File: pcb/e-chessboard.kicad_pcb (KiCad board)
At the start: 2 copper layers, 170 x 170 mm, 54 parts, among them J1 POWER, J2 UART, Q1 BC847, Q2 BC847, SW1 Reset, SW2 Boot, U1 ESP32-WROOM-32U, U2 AOZ1280, U3 NCV7608

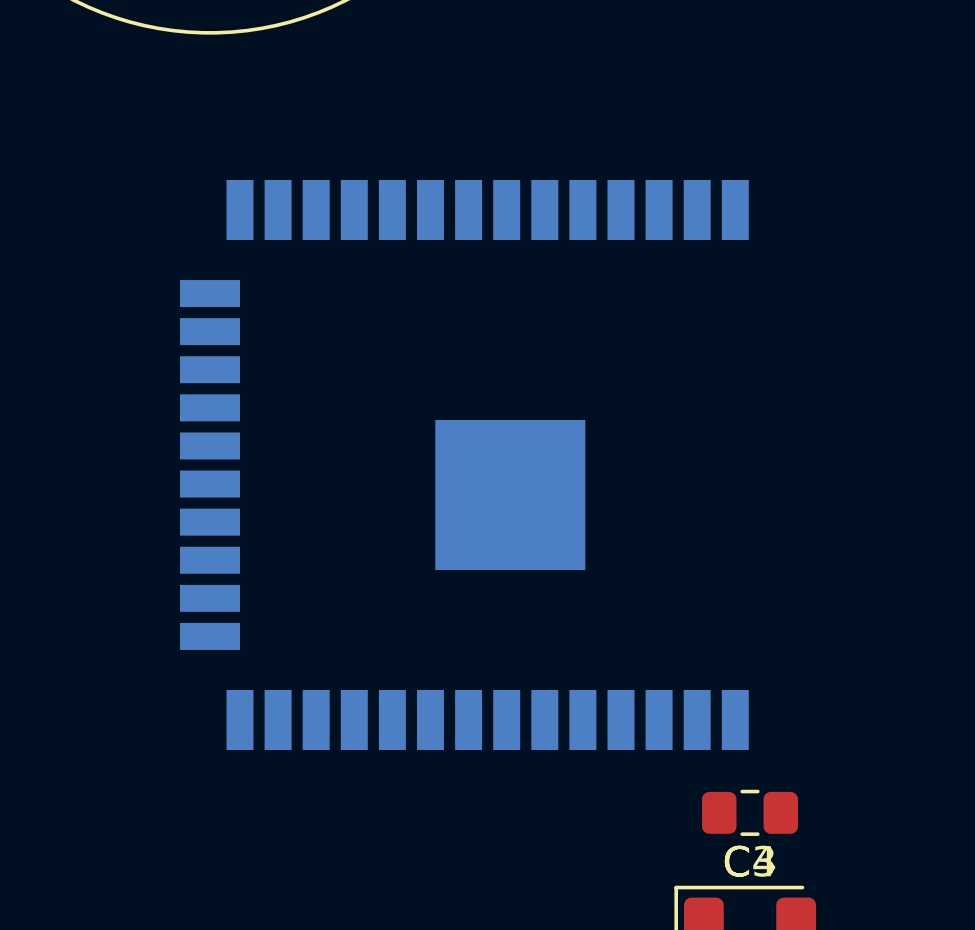
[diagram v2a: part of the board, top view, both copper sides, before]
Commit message: fix(kicad): fixing pin order of pwm
Adjusting the pin order of the pwm lines for better line laying.
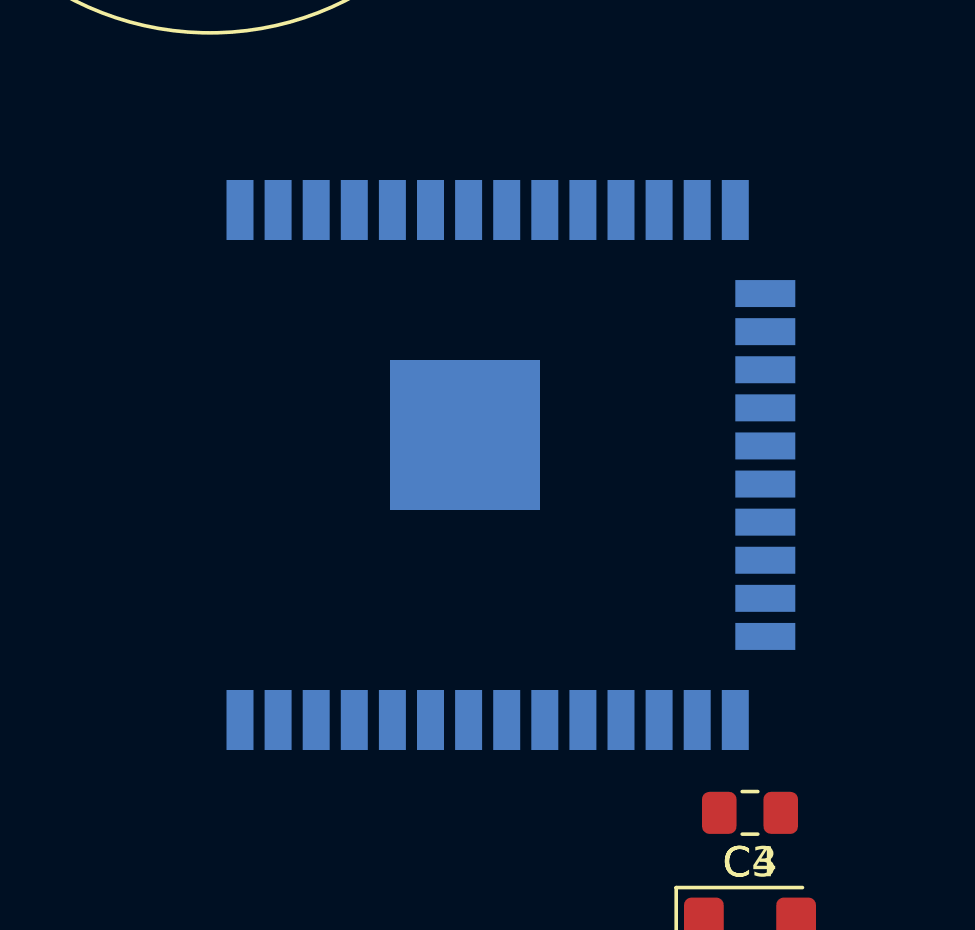
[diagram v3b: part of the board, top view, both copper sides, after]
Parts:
- turned U1 to 270 degrees
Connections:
- U1 pad 12: MAG_PWM_ROW3 -> MAG_PWM_ROW1
- U1 pad 8: MAG_PWM_ROW1 -> MAG_PWM_ROW3

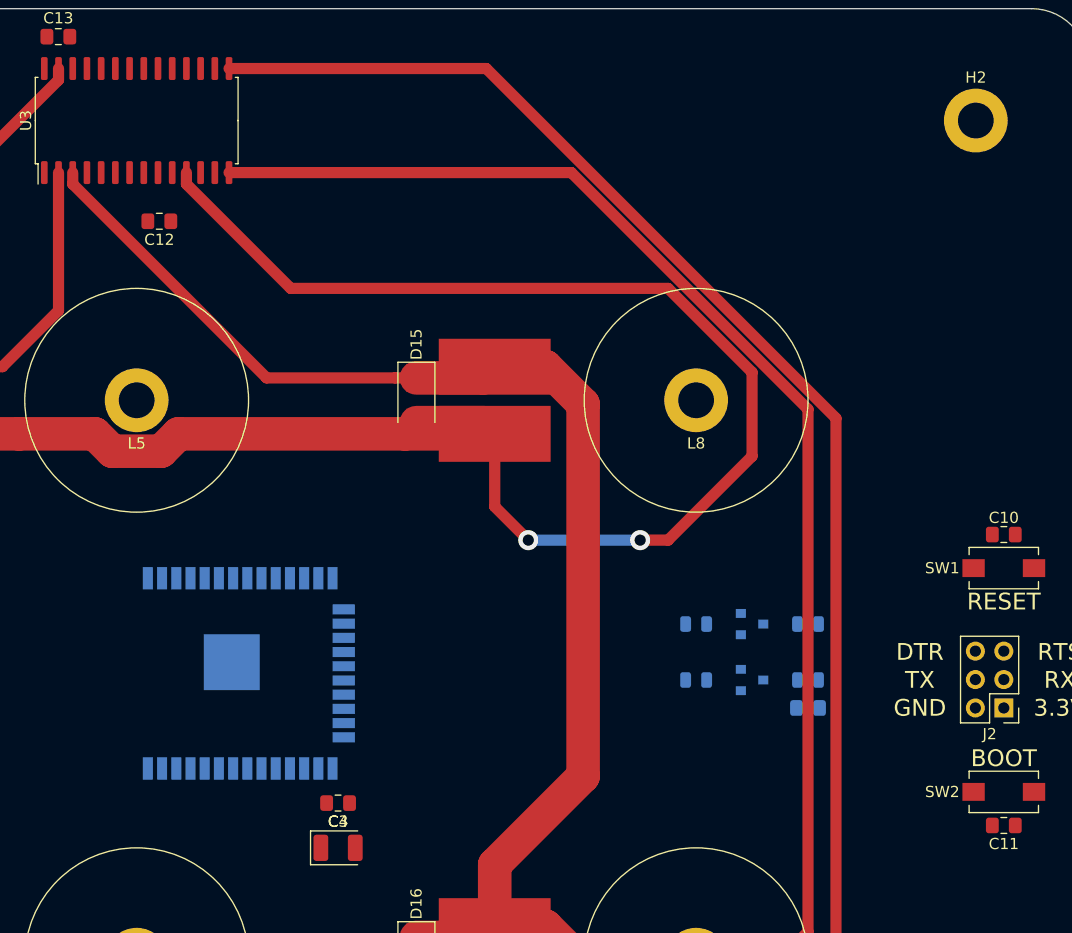
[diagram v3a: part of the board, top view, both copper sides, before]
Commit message: feat(kicad): wireing mosfet driver
Completly wirering the mosfet driver ic.
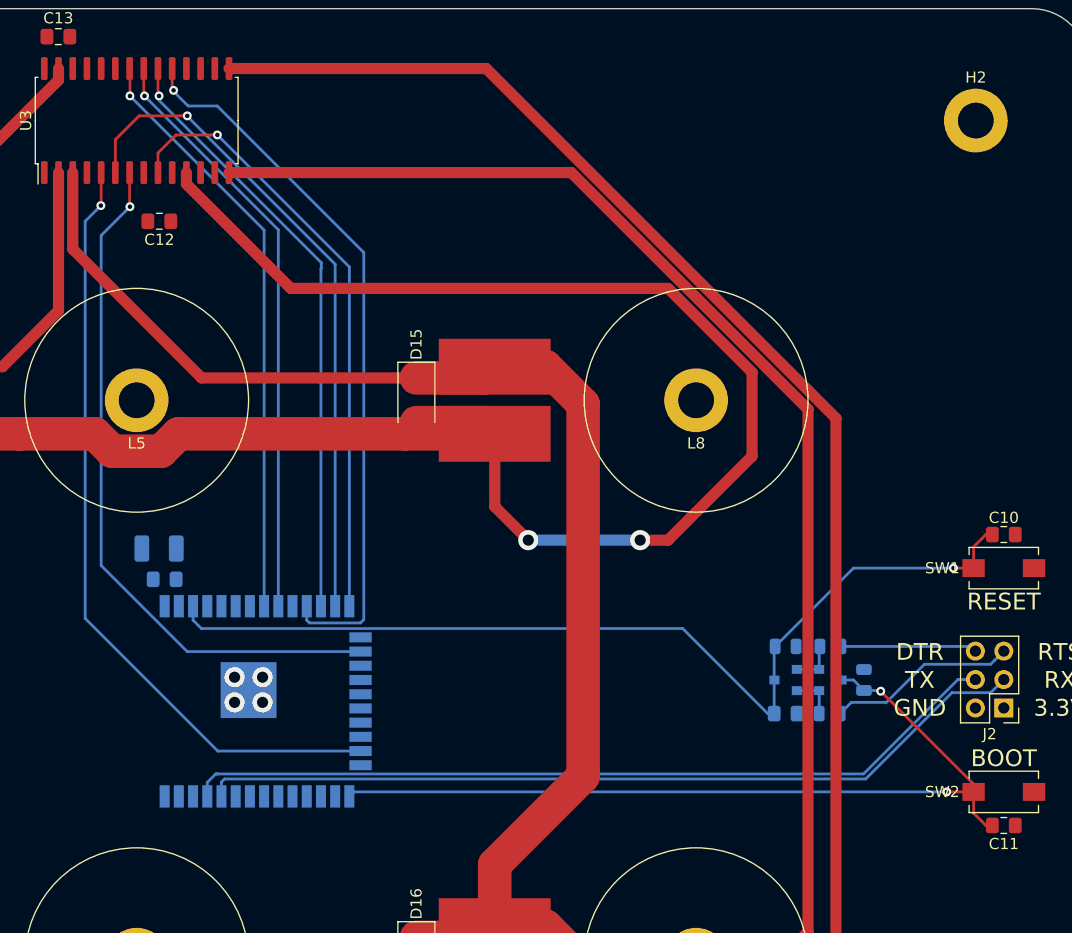
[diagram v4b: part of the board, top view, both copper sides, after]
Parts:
- C3, C4: moved to B.Cu
- moved C3 31.2 mm to (137.0, 98.2), turned to 180 degrees
- moved C4 25.3 mm to (137.5, 101.0), turned to 0 degrees
- moved R2 14.4 mm to (196.9, 113.0), turned to 0 degrees
- moved R1 12.4 mm to (197.0, 107.0), turned to 0 degrees
- moved Q2 8.60 mm to (197.0, 110.0)
- moved R6 7.07 mm to (200.0, 110.0), turned to 90 degrees
- moved R5 3.61 mm to (193.0, 107.0), turned to 0 degrees
- moved Q1 3.00 mm to (193.0, 110.0), turned to 180 degrees
- moved U1 2.92 mm to (145.8, 111.9)
- moved C9 2.06 mm to (193.0, 113.0), turned to 0 degrees
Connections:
- U1 pad 11: (no net) -> MAG_EN
- U1 pad 27: MAG_EN -> (no net)
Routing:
- net EN: track 0.00 -> 87.3 mm, vias 0 -> 1
- net IO0: track 0.00 -> 76.3 mm, vias 0 -> 2
- net UART_RX: track 0.00 -> 75.0 mm
- net UART_TX: track 0.00 -> 73.7 mm
- net MAG_CS: track 0.00 -> 70.0 mm, vias 0 -> 1
- net MAG_EN: track 0.00 -> 64.4 mm, vias 0 -> 1
- net MOSI: track 0.00 -> 62.6 mm, vias 0 -> 1
- net SCLK: track 0.00 -> 59.6 mm, vias 0 -> 1
- net MISO: track 0.00 -> 54.7 mm, vias 0 -> 1
- net MAG_PWM_ROW1: track 0.00 -> 54.1 mm, vias 0 -> 1
- net MAG_PWM_ROW2: track 0.00 -> 53.0 mm, vias 0 -> 1
- net MAG_PWM_ROW3: track 0.00 -> 53.0 mm, vias 0 -> 1
- net RTS: track 0.00 -> 16.9 mm
- net DTR: track 0.00 -> 12.2 mm
- net Net-(Q1-Pad1): track 0.00 -> 4.08 mm
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
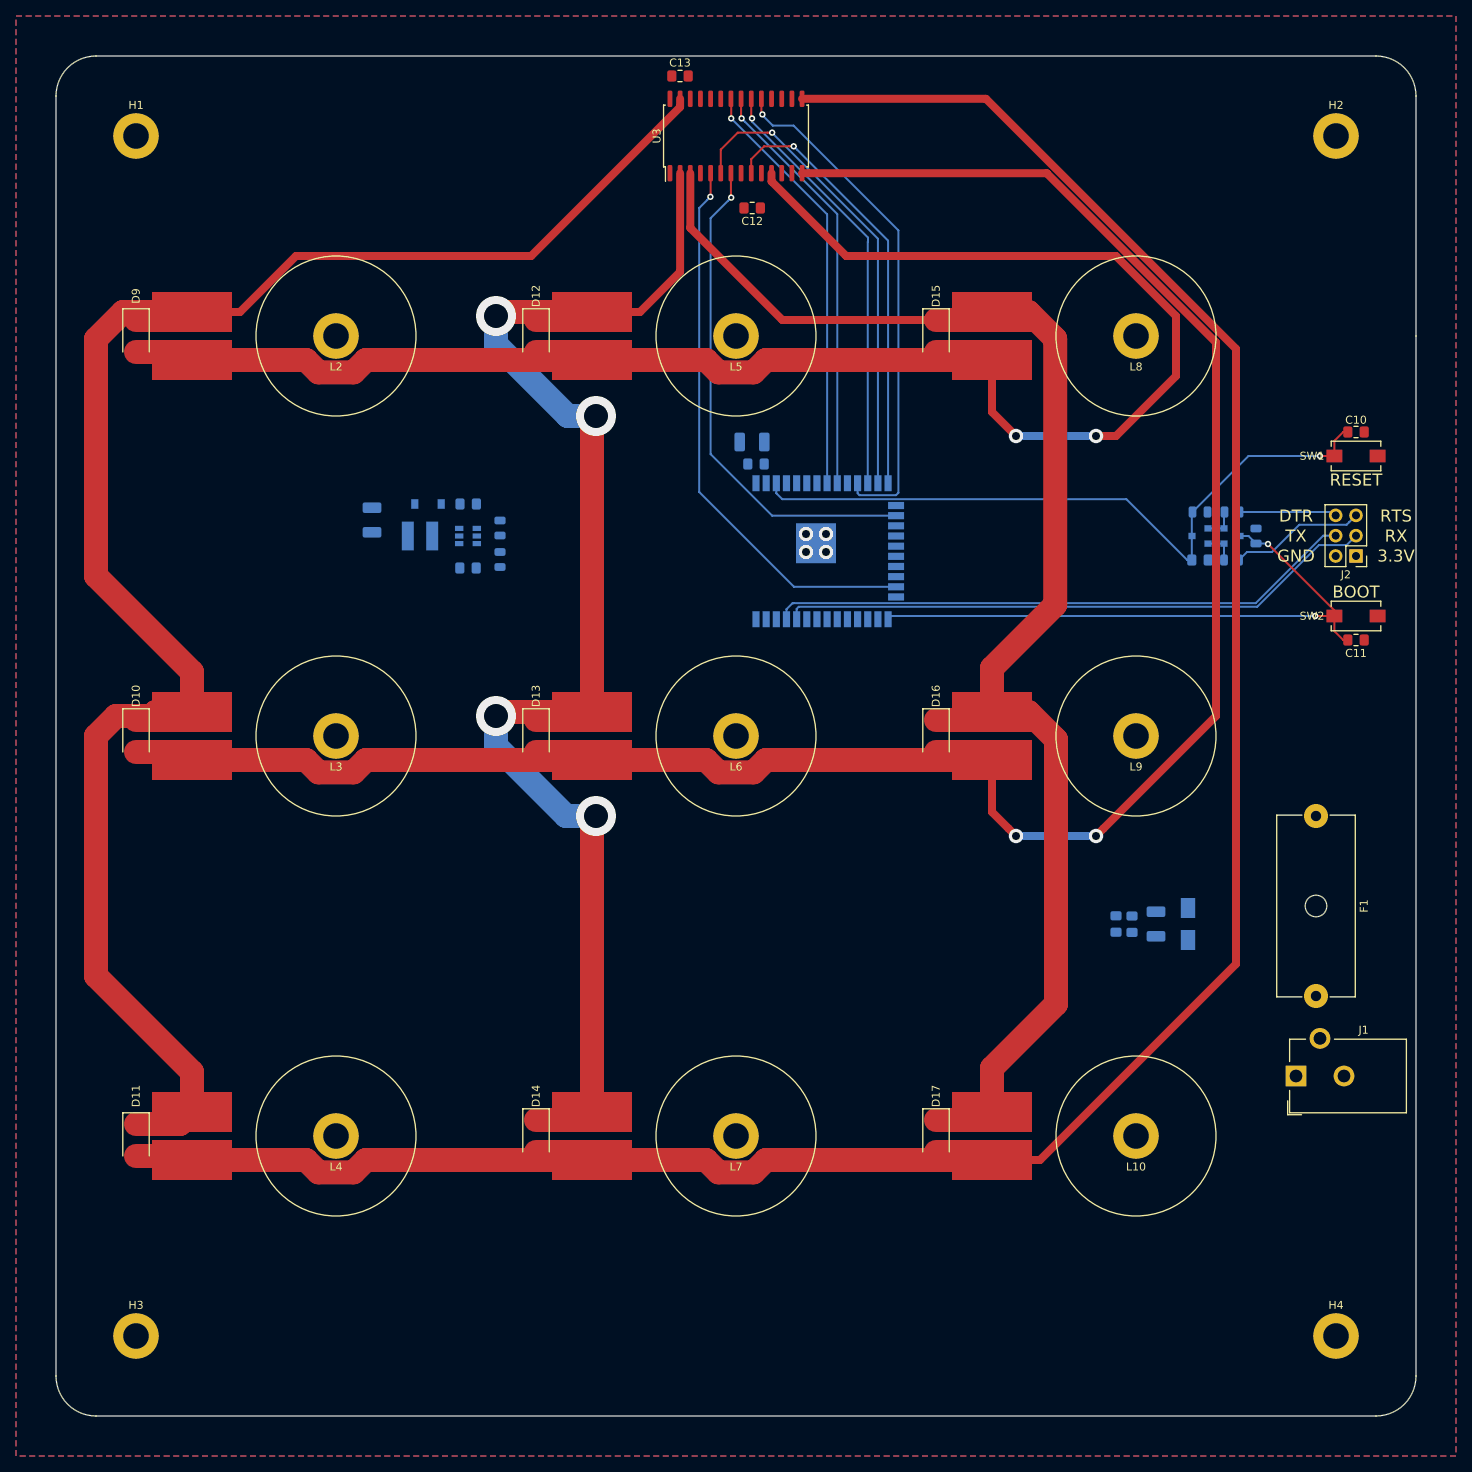
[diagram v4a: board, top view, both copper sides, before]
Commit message: feat(kicad): adding 0R resistor for programmer safty
Adding a zero ohm resistor between the buck converter and the progrmamer
3.3v line for safty reasons.
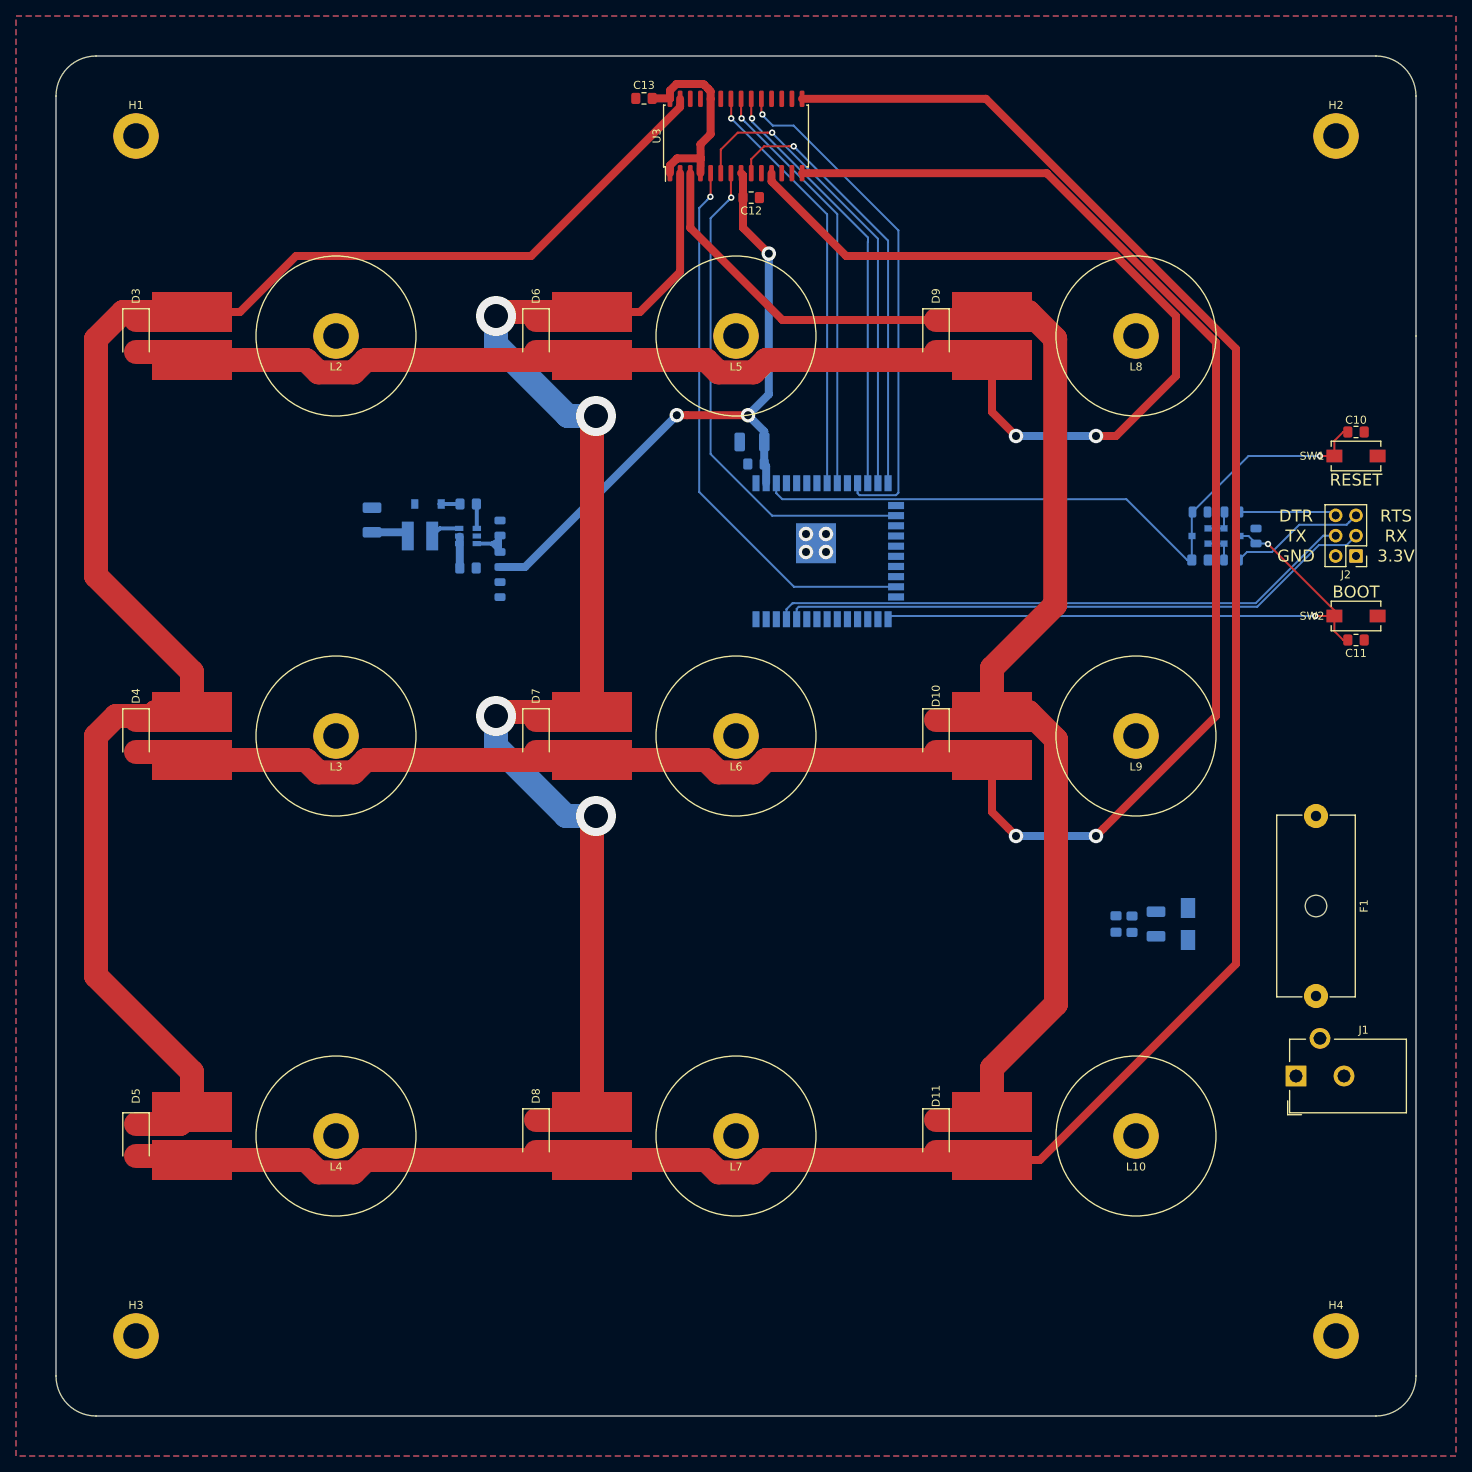
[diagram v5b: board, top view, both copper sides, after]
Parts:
- added R7: 0, Resistor_SMD:R_0805_2012Metric, B.Cu at (105.5, 116.7)
- moved C13 5.30 mm to (123.5, 55.3)
- moved C12 1.31 mm to (136.9, 67.7)
- renumbered D3 to D1, D16 to D10, D17 to D11, D8 to D2, D9 to D3, D10 to D4, D11 to D5, D12 to D6, D13 to D7, D14 to D8, D15 to D9
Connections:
- J2 pad 1: +3V3 -> Net-(J2-Pad1)
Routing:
- net +3V3: track 0.00 -> 85.7 mm, vias 0 -> 3
- net +12V: track 0.00 -> 33.0 mm
- net Net-(R3-Pad2): track 0.00 -> 8.61 mm
- net Net-(L1-Pad1): track 0.00 -> 3.77 mm
- net Net-(C7-Pad2): track 0.00 -> 3.07 mm
- net Net-(C7-Pad1): track 0.00 -> 2.60 mm
